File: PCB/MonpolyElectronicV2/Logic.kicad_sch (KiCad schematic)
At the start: 55 parts, among them J1 Conn_01x14, J3 2171820001, J4 Conn_01x05, J5 Conn_01x04, J6 Conn_01x10, J7 Conn_01x05, Q1 NPN, Q2 NPN, Q3 AO3400A, Q4 AO3401A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

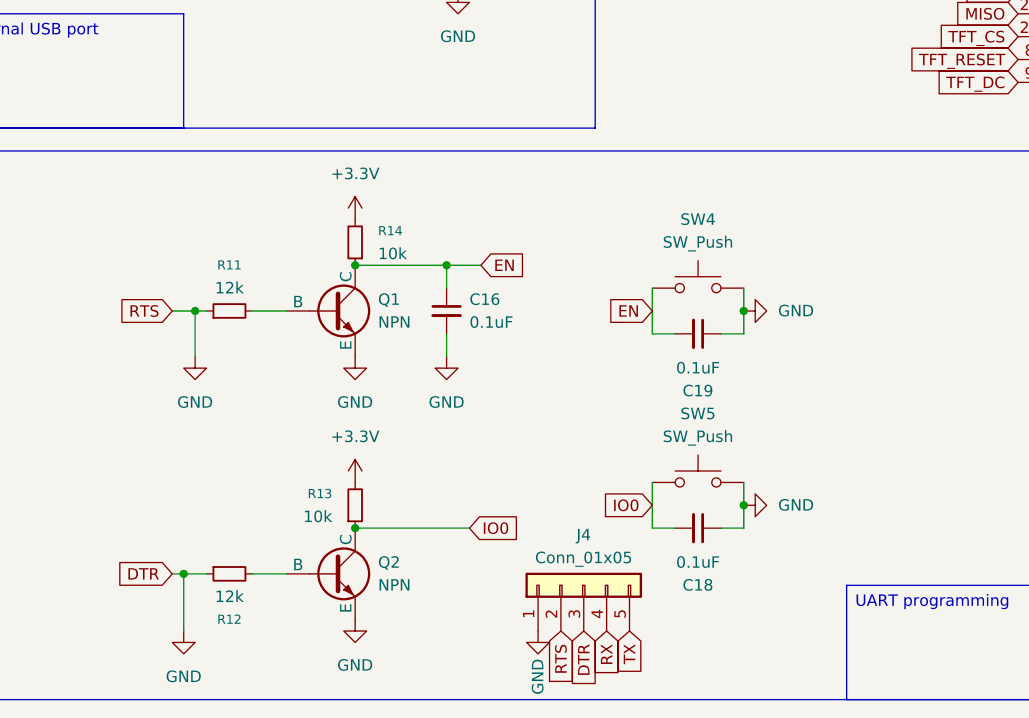
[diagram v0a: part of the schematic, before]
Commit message: fix DTR and RTS circuit
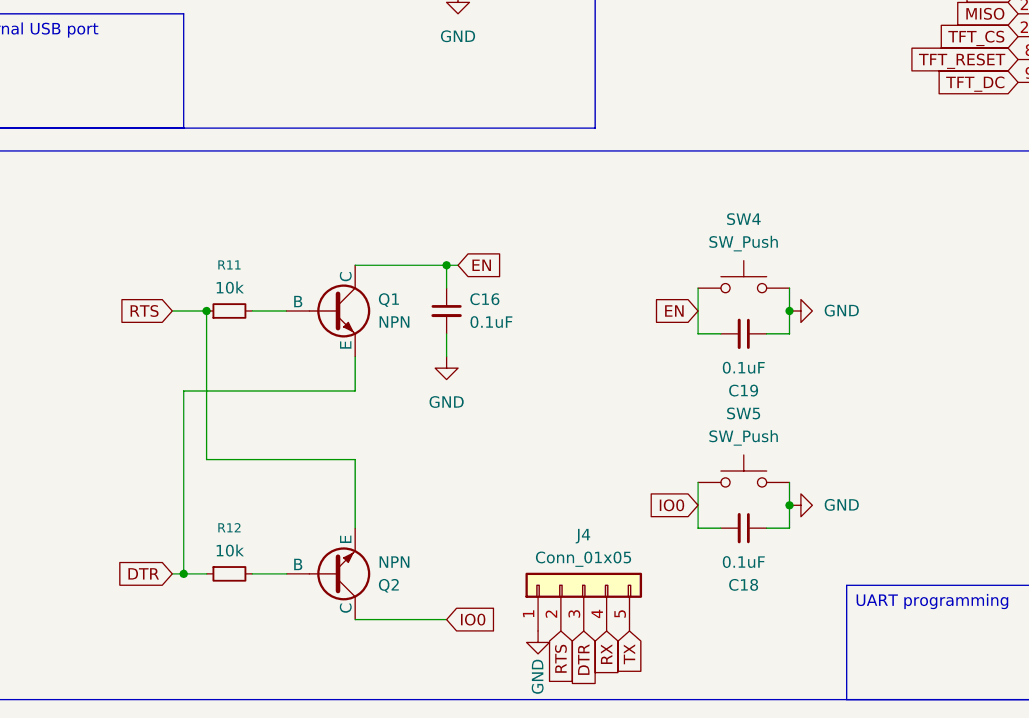
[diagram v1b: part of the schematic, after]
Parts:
- removed R13, R14: 10k, Resistor_SMD:R_0603_1608Metric, symbol Device:R_Small
- R11, R12: value 12k -> 10k
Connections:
- net GND: no longer J4.2 (Pin_2), J4.3 (Pin_3), Q1.3 (E), Q2.3 (E), R11.1, R12.1
- new net DTR: J4.3 (Pin_3), Q1.3 (E), R12.1
- new net RTS: J4.2 (Pin_2), Q2.3 (E), R11.1
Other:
- moved on the sheet: C18, C19, SW4, SW5

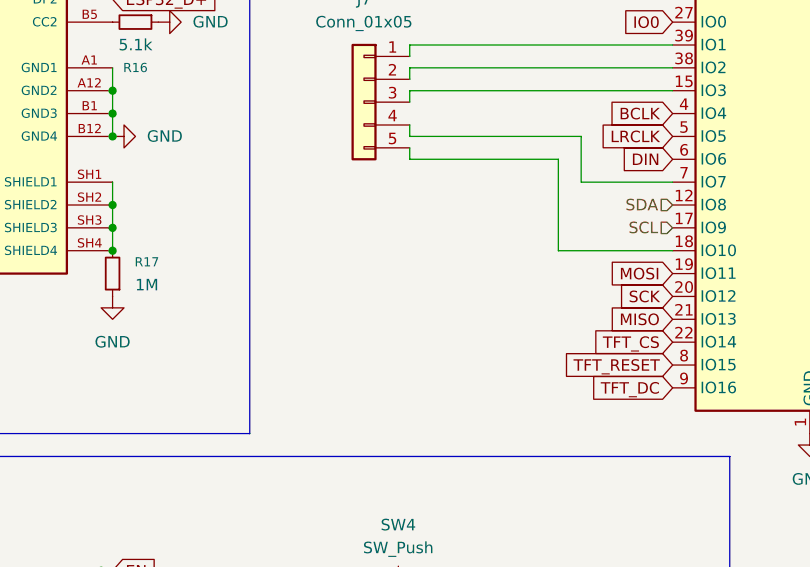
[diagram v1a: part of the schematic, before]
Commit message: Start component placing by groups: BQ25895RTWR, TPS62162DSG and 10155435-00011LF done
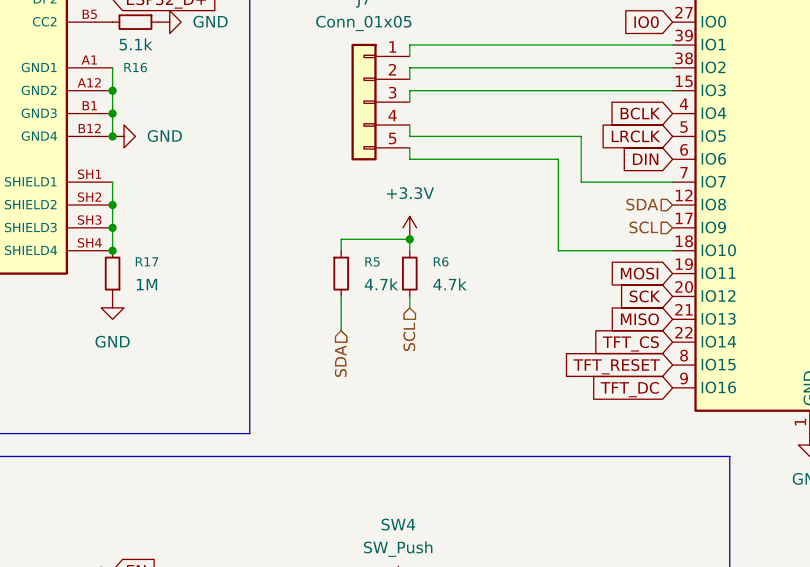
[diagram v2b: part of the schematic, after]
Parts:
- added R5, R6: 4.7k, Resistor_SMD:R_0603_1608Metric, symbol Device:R_Small
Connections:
- net +3.3V: now also R5.1, R6.1
- net SCL: now also R6.2
- net SDA: now also R5.2

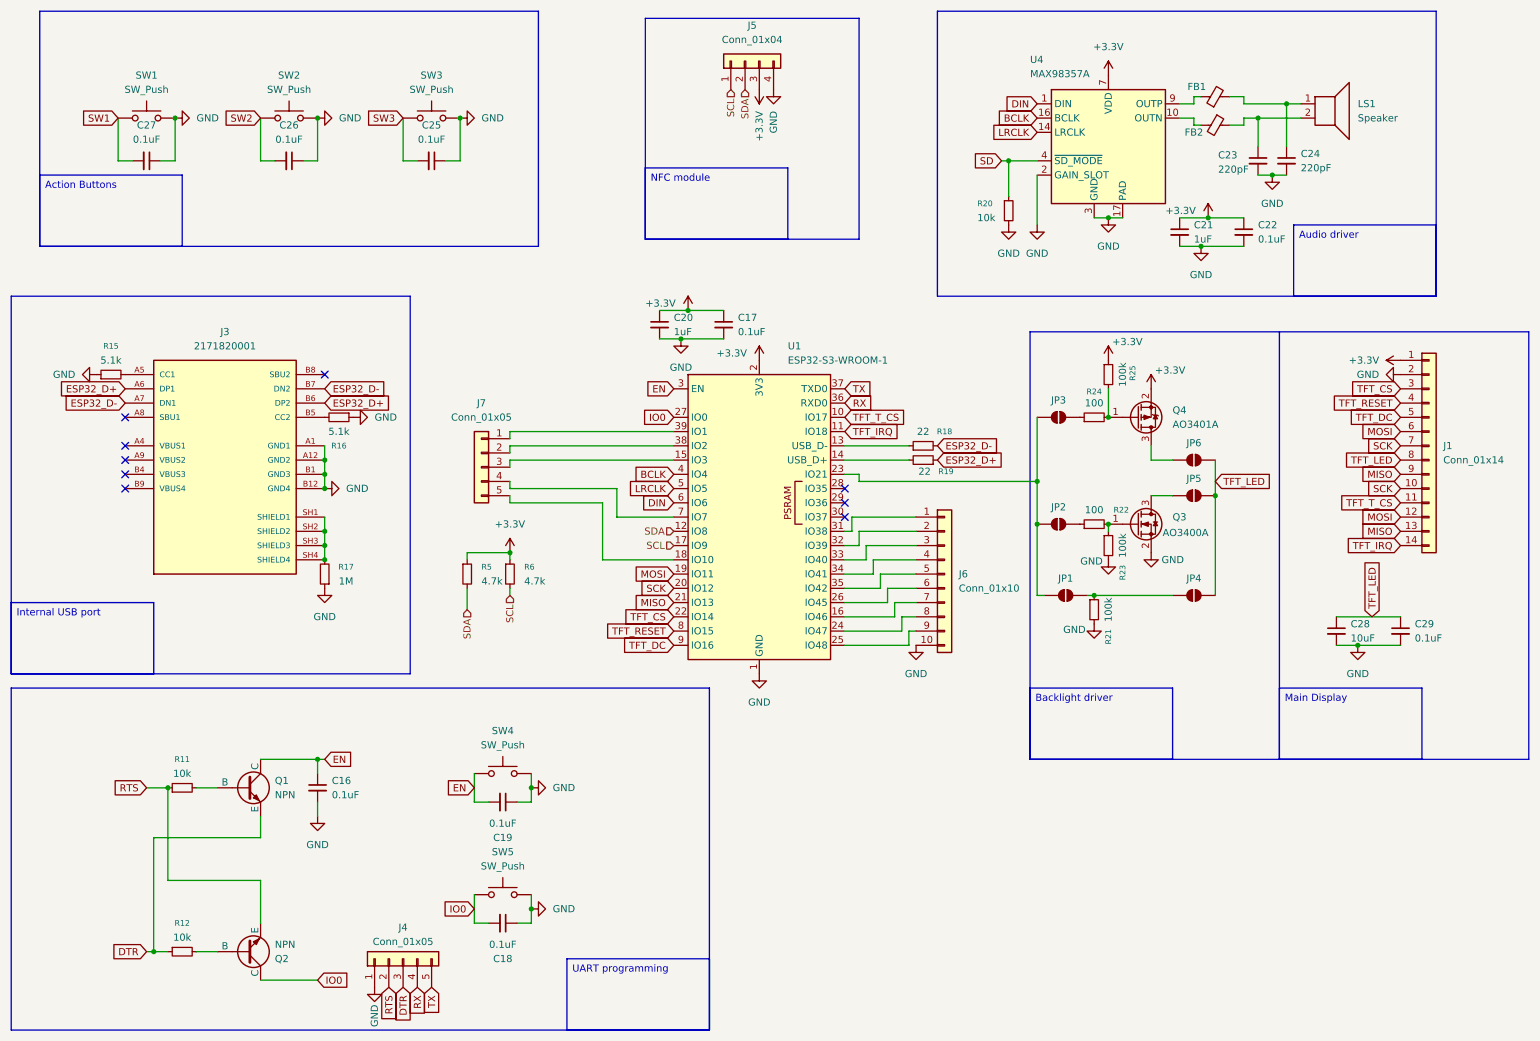
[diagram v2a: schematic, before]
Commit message: finish placement of all components
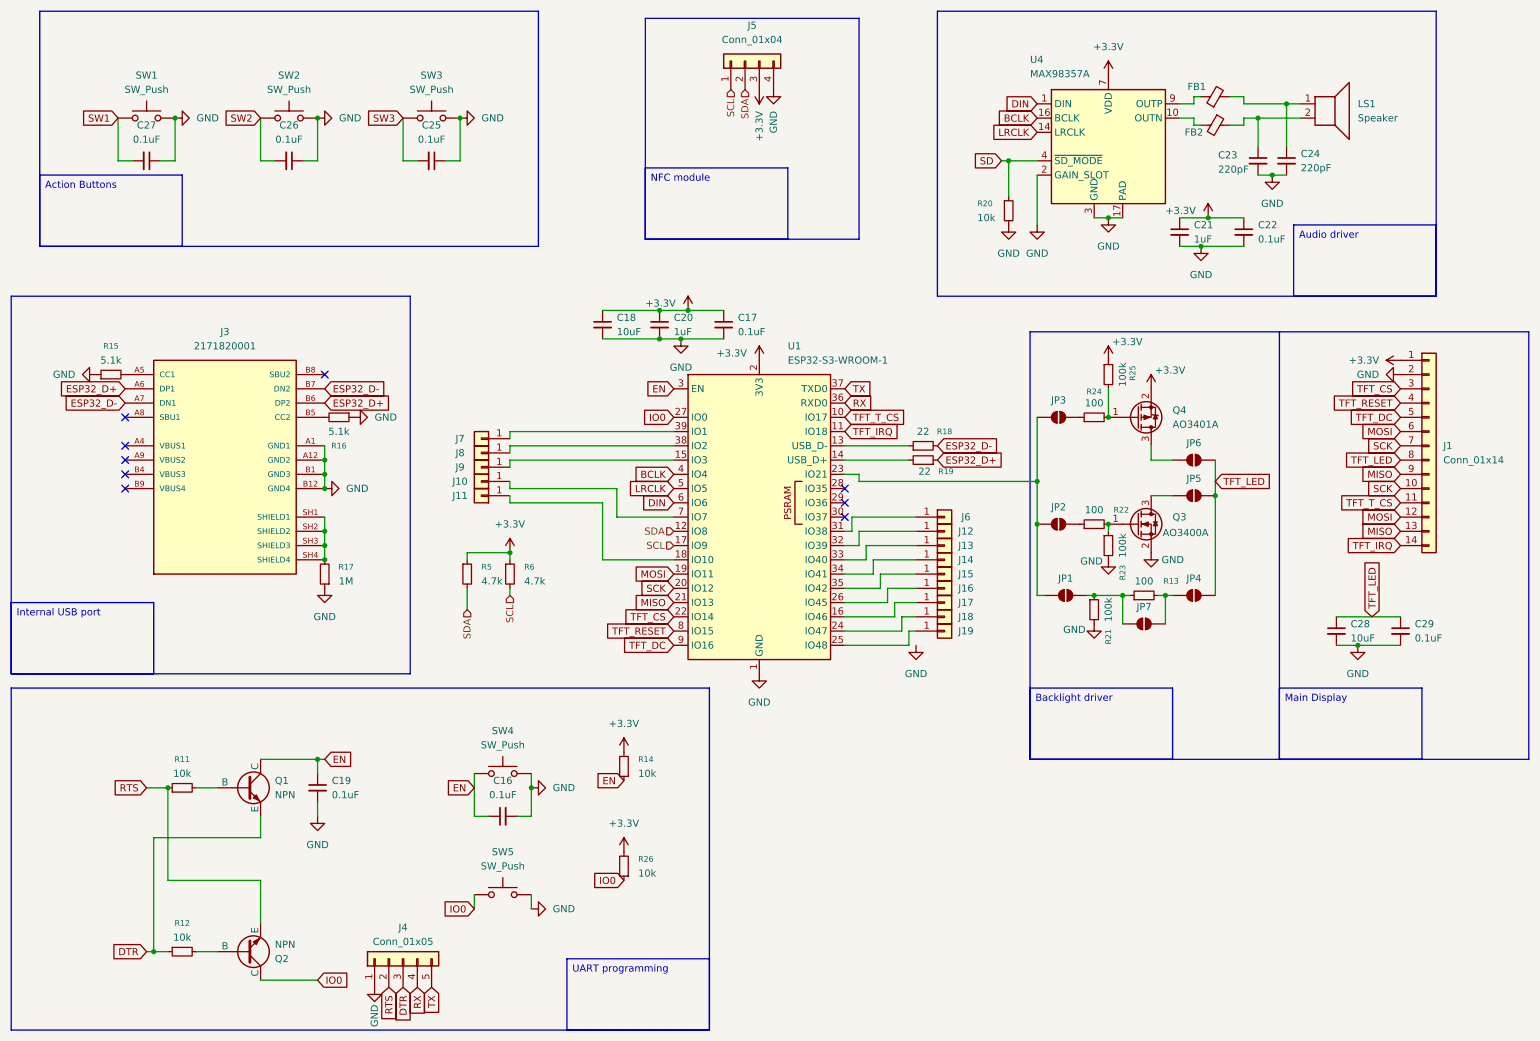
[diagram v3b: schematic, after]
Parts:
- removed J6: Conn_01x10, Connector_PinHeader_2.54mm:PinHeader_1x10_P2.54mm_Vertical, symbol Connector_Generic:Conn_01x10
- removed J7: Conn_01x05, Connector_PinHeader_2.54mm:PinHeader_1x05_P2.54mm_Vertical, symbol Connector_Generic:Conn_01x05
- added J10, J11, J12, J13, J14, J15, J16, J17, J18, J19, J6, J7, J8, J9: Conn_01x01, Connector_PinHeader_2.54mm:PinHeader_1x01_P2.54mm_Vertical, symbol Connector_Generic:Conn_01x01
- added JP7: SolderJumper_2_Open, Jumper:SolderJumper-2_P1.3mm_Open_TrianglePad1.0x1.5mm, symbol Jumper:SolderJumper_2_Open
- added R13: 100, Resistor_SMD:R_0603_1608Metric, symbol Device:R_Small
- added R14, R26: 10k, Resistor_SMD:R_0603_1608Metric, symbol Device:R_Small
- C18: value 0.1uF -> 10uF
- SW1, SW2, SW3: footprint Button_Switch_THT:SW_PUSH-12mm -> Extra:SW_TL1105BF160Q
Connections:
- net +3.3V: now also C18.1, R14.2, R26.2
- net EN: now also C19.1, R14.1; no longer C19.2
- net GND: now also C18.2, C19.2; no longer C18.1, C19.1
- net IO0: now also R26.1; no longer C18.2
- net at U1.15 (IO3): now also J9.1 (Pin_1)
- net at U1.16 (IO46): now also J17.1 (Pin_1)
- net at U1.18 (IO10): now also J11.1 (Pin_1)
- net at U1.24 (IO47): now also J18.1 (Pin_1)
- net at U1.25 (IO48): now also J19.1 (Pin_1)
- net at U1.26 (IO45): now also J16.1 (Pin_1)
- net at U1.31 (IO38): now also J6.1 (Pin_1)
- net at U1.32 (IO39): now also J12.1 (Pin_1)
- net at U1.33 (IO40): now also J13.1 (Pin_1)
- net at U1.34 (IO41): now also J14.1 (Pin_1)
- net at U1.35 (IO42): now also J15.1 (Pin_1)
- net at U1.38 (IO2): now also J8.1 (Pin_1)
- net at U1.39 (IO1): now also J7.1 (Pin_1)
- net at U1.7 (IO7): now also J10.1 (Pin_1)
- net at JP1.1 (A), R21.1: now also JP7.2 (B), R13.1; no longer JP4.2 (B)
- new net: JP4.2 (B), JP7.1 (A), R13.2
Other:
- moved on the sheet: C16, C19

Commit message: finish placing components
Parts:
- J1: footprint Connector_PinHeader_2.54mm:PinHeader_1x14_P2.54mm_Vertical -> Extra:240X320 TFT 3.2 display
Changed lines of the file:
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@@
 			)
 		)
-		(property "Footprint" "Connector_PinHeader_2.54mm:PinHeader_1x14_P2.54mm_Vertical"
+		(property "Footprint" "Extra:240X320 TFT 3.2 display"
 			(at 265.43 90.17 0)
 			(effects

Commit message: Finish routing PCB
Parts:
- removed J11, J17, J6, J9: Conn_01x01, Connector_PinHeader_2.54mm:PinHeader_1x01_P2.54mm_Vertical, symbol Connector_Generic:Conn_01x01
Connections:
- net SW1: now also U1.15 (IO3)
- net SW2: now also U1.18 (IO10)
- net SW3: now also U1.16 (IO46)
- net TFT_RESET: now also U1.31 (IO38); no longer U1.8 (IO15)
